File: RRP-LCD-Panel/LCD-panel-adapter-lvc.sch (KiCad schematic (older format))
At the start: 8 parts, among them J101 HEADER_18, P101 CONN_4X2, P102 CONN_5X2, P103 CONN_5X2, U101 SN74LVCC4245A

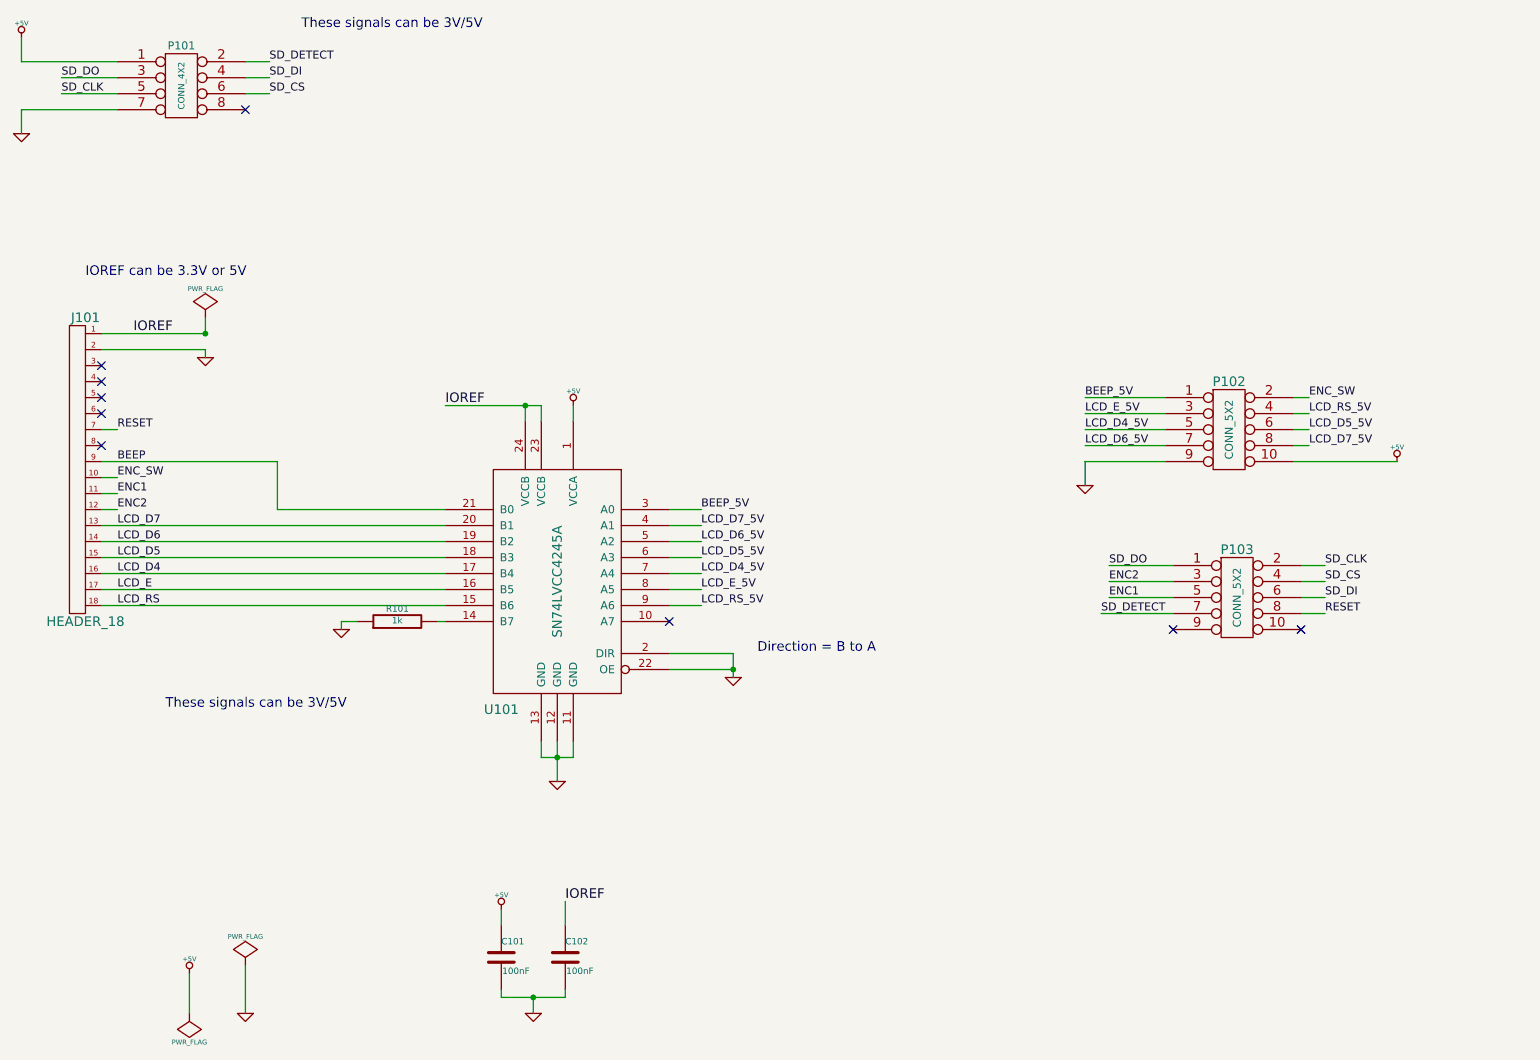
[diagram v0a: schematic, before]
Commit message: LCD Panel adapter: use 74HC07
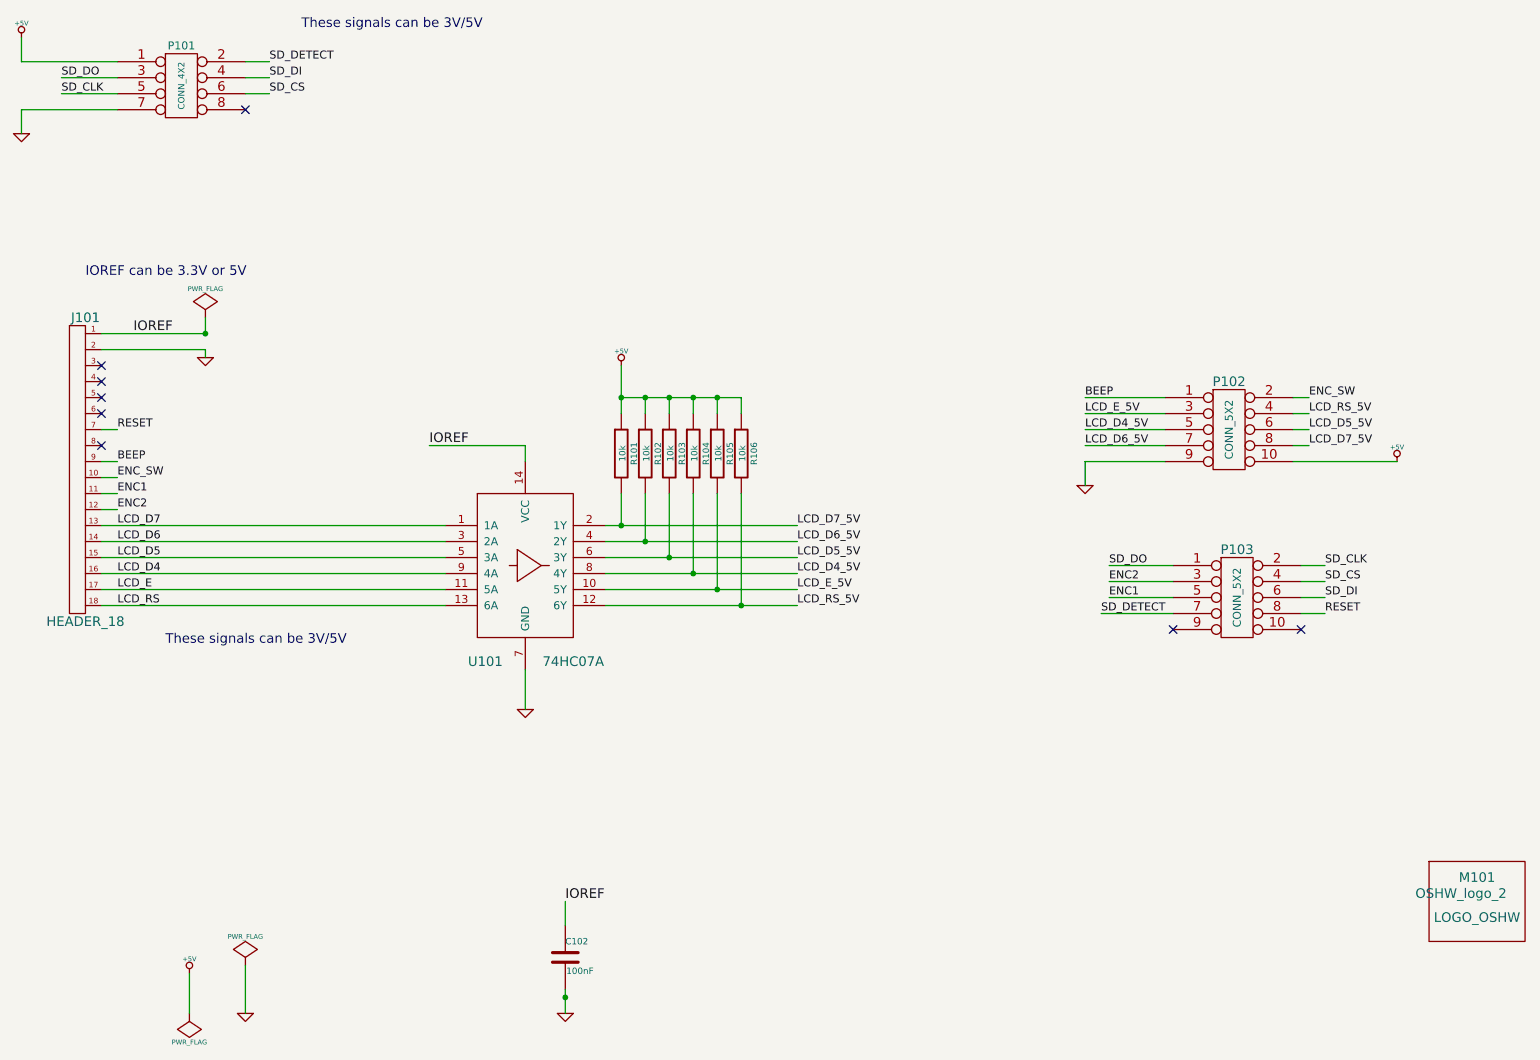
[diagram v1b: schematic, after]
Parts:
- removed C101: 100nF, ~, symbol C
- removed U101: SN74LVCC4245A, ~, symbol 74LVC4245
- added M101: LOGO_OSHW, OSHW_logo_2, symbol LOGO_OSHW
- added R102, R103, R104, R105, R106: 10k, ~, symbol R
- added U101: 74HC07A, ~, symbol 74LVC07A
- R101: value 1k -> 10k
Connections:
- net BEEP_5V is gone; now on net BEEP: P102.1
- net +5V: now also R101.1, R102.1, R103.1, R104.1, R105.1, R106.1
- net GND: now also U101.7 (GND); no longer R101.1
- net IOREF: now also U101.14 (VCC)
- net LCD_D4: now also U101.9 (4A)
- net LCD_D4_5V: now also R104.2, U101.8 (4Y)
- net LCD_D5: now also U101.5 (3A)
- net LCD_D5_5V: now also R103.2, U101.6 (3Y)
- net LCD_D6: now also U101.3 (2A)
- net LCD_D6_5V: now also R102.2, U101.4 (2Y)
- net LCD_D7: now also U101.1 (1A)
- net LCD_D7_5V: now also R101.2, U101.2 (1Y)
- net LCD_E: now also U101.11 (5A)
- net LCD_E_5V: now also R105.2, U101.10 (5Y)
- net LCD_RS: now also U101.13 (6A)
- net LCD_RS_5V: now also R106.2, U101.12 (6Y)
- no-connect marks 9 -> 8
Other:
- note removed: "Direction = B to A"
